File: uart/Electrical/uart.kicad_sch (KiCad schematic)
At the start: 18 parts, among them P2 USB_C_Plug, U1 AP2112K-3.3, U2 FT232RL

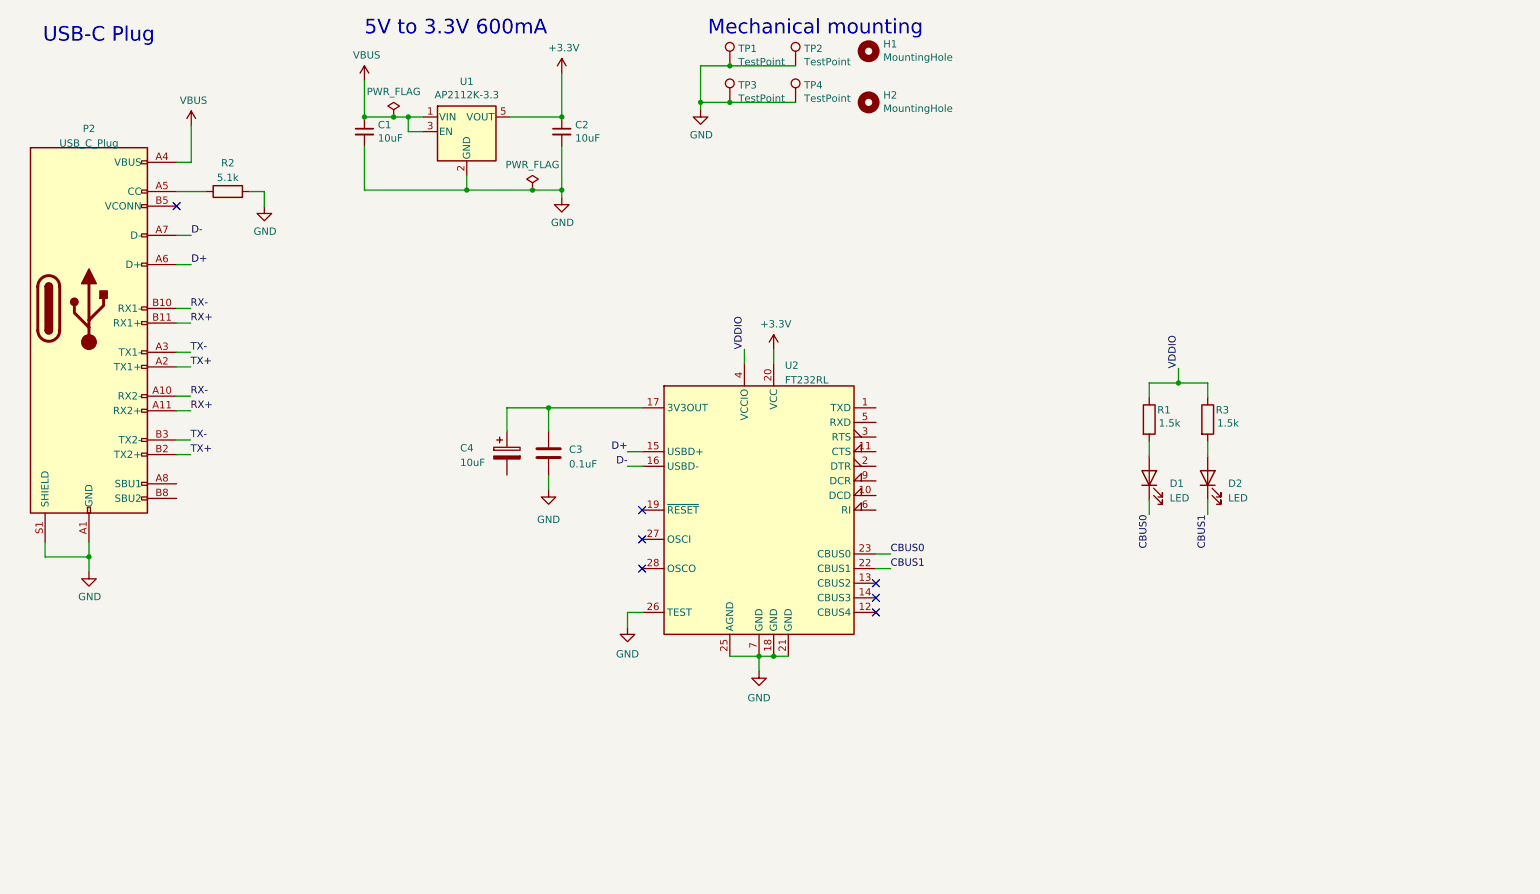
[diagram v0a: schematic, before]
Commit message: Updated uart schematic
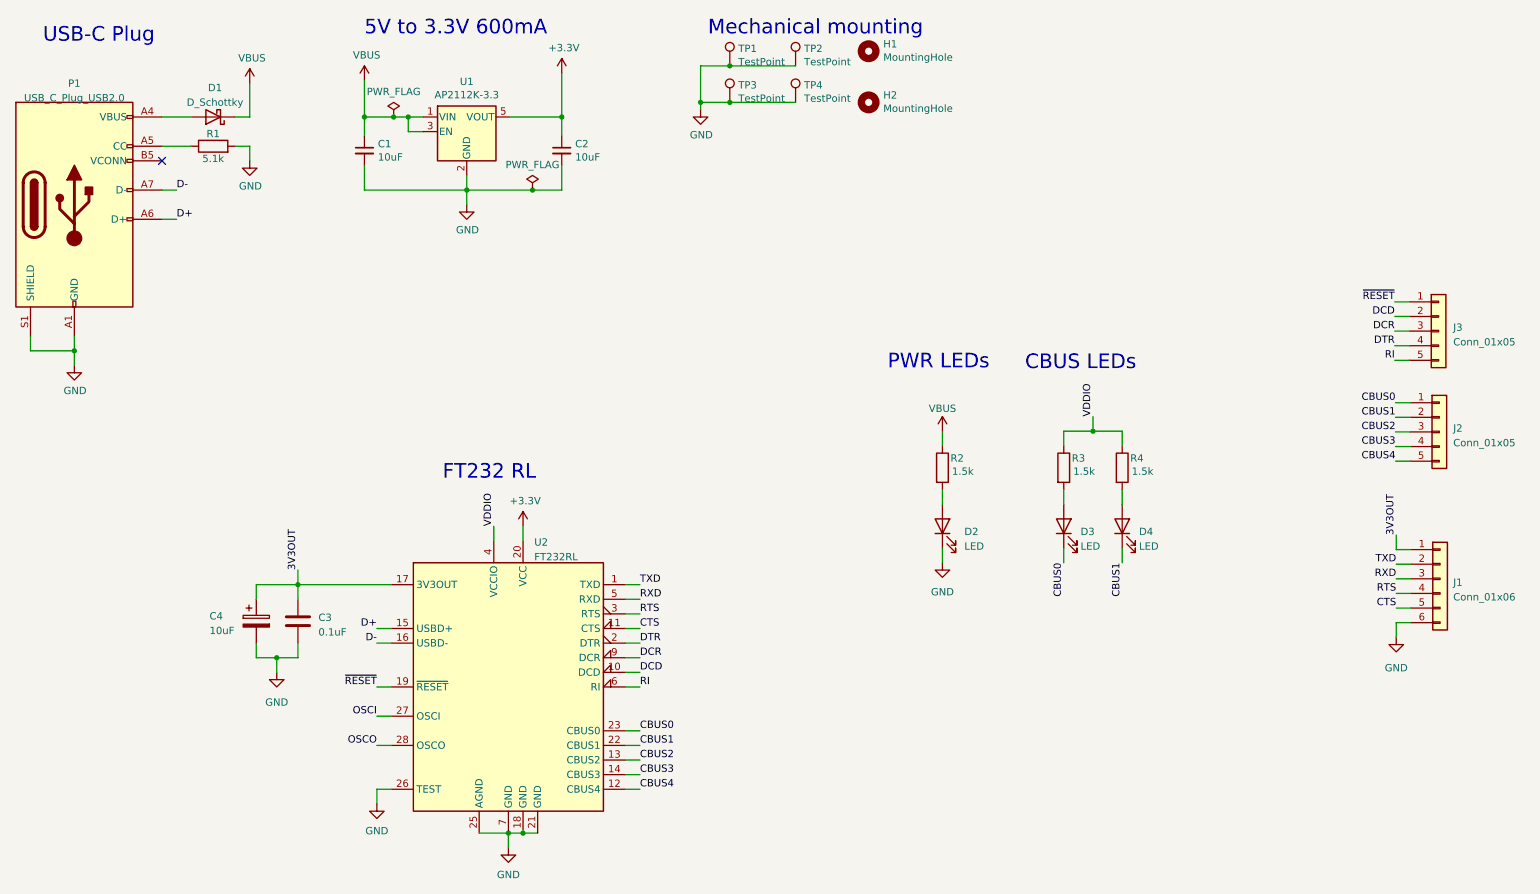
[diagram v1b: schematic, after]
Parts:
- removed P2: USB_C_Plug, Connector_USB:USB_C_Plug_Molex_105444, symbol Connector:USB_C_Plug
- added D1: D_Schottky, Diode_SMD:D_0201_0603Metric, symbol Device:D_Schottky
- added D2: LED, LED_SMD:LED_0201_0603Metric, symbol Device:LED
- added J1: Conn_01x06, Connector_PinHeader_2.00mm:PinHeader_1x06_P2.00mm_Horizontal, symbol Connector_Generic:Conn_01x06
- added J2, J3: Conn_01x05, Connector_PinHeader_2.00mm:PinHeader_1x05_P2.00mm_Vertical, symbol Connector_Generic:Conn_01x05
- added P1: USB_C_Plug_USB2.0, symbol Connector:USB_C_Plug_USB2.0
- added R1: 5.1k, Resistor_SMD:R_0201_0603Metric, symbol Device:R
- R2: value 5.1k -> 1.5k
- TP1, TP2, TP3, TP4: footprint TestPoint:TestPoint_Pad_1.5x1.5mm -> (none)
- renumbered D1 to D3, D2 to D4, R1 to R3, R3 to R4
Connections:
- net CBUS0: now also J2.1 (Pin_1)
- net CBUS1: now also J2.2 (Pin_2)
- net D+: now also P1.A6 (D+)
- net D-: now also P1.A7 (D-)
- net GND: now also C4.2, D2.1 (K), J1.6 (Pin_6), P1.A1 (GND), P1.A12 (GND), P1.B1 (GND), P1.B12 (GND), P1.S1 (SHIELD), R1.2; no longer R2.2
- net VBUS: now also R2.1, D1.1 (K)
- net TXD: now reaches U2.1 (TXD)
- net TXD: now also J1.2 (Pin_2)
- net DCD: now reaches U2.10 (DCD)
- net DCD: now also J3.2 (Pin_2)
- net CTS: now reaches U2.11 (CTS)
- net CTS: now also J1.5 (Pin_5)
- net CBUS4: now reaches U2.12 (CBUS4)
- net CBUS4: now also J2.5 (Pin_5)
- net CBUS2: now reaches U2.13 (CBUS2)
- net CBUS2: now also J2.3 (Pin_3)
- net CBUS3: now reaches U2.14 (CBUS3)
- net CBUS3: now also J2.4 (Pin_4)
- net 3V3OUT: now reaches C3.1, C4.1, U2.17 (3V3OUT)
- net 3V3OUT: now also J1.1 (Pin_1)
- net ~{RESET}: now reaches U2.19 (~{RESET})
- net ~{RESET}: now also J3.1 (Pin_1)
- net DTR: now reaches U2.2 (DTR)
- net DTR: now also J3.4 (Pin_4)
- net OSCI: now reaches U2.27 (OSCI)
- net OSCO: now reaches U2.28 (OSCO)
- net RTS: now reaches U2.3 (RTS)
- net RTS: now also J1.4 (Pin_4)
- net RXD: now reaches U2.5 (RXD)
- net RXD: now also J1.3 (Pin_3)
- net RI: now reaches U2.6 (RI)
- net RI: now also J3.5 (Pin_5)
- net DCR: now reaches U2.9 (DCR)
- net DCR: now also J3.3 (Pin_3)
- new net: D2.2 (A), R2.2
- new net: D1.2 (A), P1.A4 (VBUS), P1.A9 (VBUS), P1.B4 (VBUS), P1.B9 (VBUS)
- new net: P1.A5 (CC), R1.1
- no-connect marks 7 -> 1
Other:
- note added: "CBUS LEDs"
- note added: "FT232 RL"
- note added: "PWR LEDs"
- company: Framework -> (none)
- moved on the sheet: C1, C2, C3, C4, D3, D4, R3, R4, U2

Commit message: Updated uart Schematic
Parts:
- removed J2, J3: Conn_01x05, Connector_PinHeader_2.00mm:PinHeader_1x05_P2.00mm_Vertical, symbol Connector_Generic:Conn_01x05
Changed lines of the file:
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@@
-    (stroke (width 0) (type default))
-  )
-  (wire (pts (xy 260.35 70.231) (xy 262.89 70.231))
     (stroke (width 0) (type default))
   )
@@
     (stroke (width 0) (type default))
   )
-  (wire (pts (xy 260.35 67.691) (xy 262.89 67.691))
-    (stroke (width 0) (type default))
-  )
-  (wire (pts (xy 260.477 90.297) (xy 263.017 90.297))
-    (stroke (width 0) (type default))
-  )
   (wire (pts (xy 83.439 152.4) (xy 83.439 149.86))
     (stroke (width 0) (type default))
@@
     (stroke (width 0) (type default))
   )
-  (wire (pts (xy 260.477 87.757) (xy 263.017 87.757))
-    (stroke (width 0) (type default))
-  )
   (wire (pts (xy 129.159 147.32) (xy 126.619 147.32))
     (stroke (width 0) (type default))
@@
     (stroke (width 0) (type default))
   )
-  (wire (pts (xy 260.35 75.311) (xy 262.89 75.311))
-    (stroke (width 0) (type default))
-  )
   (wire (pts (xy 181.737 100.33) (xy 181.737 97.79))
     (stroke (width 0) (type default))
@@
     (stroke (width 0) (type default))
   )
-  (wire (pts (xy 260.35 72.771) (xy 262.89 72.771))
-    (stroke (width 0) (type default))
-  )
   (wire (pts (xy 129.159 124.46) (xy 126.619 124.46))
     (stroke (width 0) (type default))
@@
     (stroke (width 0) (type default))
   )
-  (wire (pts (xy 260.35 65.151) (xy 262.89 65.151))
-    (stroke (width 0) (type default))
-  )
   (wire (pts (xy 83.439 137.16) (xy 85.979 137.16))
     (stroke (width 0) (type default))
@@
     (stroke (width 0) (type default))
   )
-  (wire (pts (xy 260.477 92.837) (xy 263.017 92.837))
-    (stroke (width 0) (type default))
-  )
-  (wire (pts (xy 260.477 85.217) (xy 263.017 85.217))
-    (stroke (width 0) (type default))
-  )
   (wire (pts (xy 83.439 132.08) (xy 85.979 132.08))
     (stroke (width 0) (type default))
@@
   )
   (wire (pts (xy 69.723 114.3) (xy 69.723 116.84))
-    (stroke (width 0) (type default))
-  )
-  (wire (pts (xy 260.477 82.677) (xy 263.017 82.677))
     (stroke (width 0) (type default))
   )
@@
     (effects (font (size 1.27 1.27)) (justify left bottom))
   )
-  (label "CBUS3" (at 260.477 90.297 180) (fields_autoplaced)
-    (effects (font (size 1.27 1.27)) (justify right bottom))
-  )
-  (label "RI" (at 260.35 75.311 180) (fields_autoplaced)
-    (effects (font (size 1.27 1.27)) (justify right bottom))
-  )
   (label "CBUS0" (at 202.819 110.49 270) (fields_autoplaced)
     (effects (font (size 1.27 1.27)) (justify right bottom))
   )
-  (label "~{RESET}" (at 260.35 65.151 180) (fields_autoplaced)
-    (effects (font (size 1.27 1.27)) (justify right bottom))
-  )
   (label "DCR" (at 129.159 127 0) (fields_autoplaced)
     (effects (font (size 1.27 1.27)) (justify left bottom))
@@
   (label "D-" (at 48.641 45.72 0) (fields_autoplaced)
     (effects (font (size 1.27 1.27)) (justify left bottom))
-  )
-  (label "DTR" (at 260.35 72.771 180) (fields_autoplaced)
-    (effects (font (size 1.27 1.27)) (justify right bottom))
   )
   (label "~{RESET}" (at 83.439 132.08 180) (fields_autoplaced)
@@
     (effects (font (size 1.27 1.27)) (justify left bottom))
   )
-  (label "DCR" (at 260.35 70.231 180) (fields_autoplaced)
-    (effects (font (size 1.27 1.27)) (justify right bottom))
-  )
   (label "CTS" (at 129.159 121.92 0) (fields_autoplaced)
     (effects (font (size 1.27 1.27)) (justify left bottom))
@@
     (effects (font (size 1.27 1.27)) (justify right bottom))
   )
-  (label "DCD" (at 260.35 67.691 180) (fields_autoplaced)
-    (effects (font (size 1.27 1.27)) (justify right bottom))
-  )
   (label "3V3OUT" (at 260.604 105.664 90) (fields_autoplaced)
     (effects (font (size 1.27 1.27)) (justify left bottom))
-  )
-  (label "CBUS1" (at 260.477 85.217 180) (fields_autoplaced)
-    (effects (font (size 1.27 1.27)) (justify right bottom))
   )
   (label "CBUS0" (at 129.159 139.7 0) (fields_autoplaced)
@@
     (effects (font (size 1.27 1.27)) (justify right bottom))
   )
-  (label "CBUS4" (at 260.477 92.837 180) (fields_autoplaced)
-    (effects (font (size 1.27 1.27)) (justify right bottom))
-  )
   (label "D+" (at 48.641 50.8 0) (fields_autoplaced)
     (effects (font (size 1.27 1.27)) (justify left bottom))
@@
     (effects (font (size 1.27 1.27)) (justify right bottom))
   )
-  (label "CBUS2" (at 260.477 87.757 180) (fields_autoplaced)
-    (effects (font (size 1.27 1.27)) (justify right bottom))
-  )
   (label "CBUS2" (at 129.159 144.78 0) (fields_autoplaced)
     (effects (font (size 1.27 1.27)) (justify left bottom))
@@
   (label "DTR" (at 129.159 124.46 0) (fields_autoplaced)
     (effects (font (size 1.27 1.27)) (justify left bottom))
-  )
-  (label "CBUS0" (at 260.477 82.677 180) (fields_autoplaced)
-    (effects (font (size 1.27 1.27)) (justify right bottom))
   )
   (label "OSCO" (at 83.439 142.24 180) (fields_autoplaced)
@@
         (path "/21020eba-b649-4135-9bee-384d0a5cab58"
           (reference "R4") (unit 1)
-        )
-      )
-    )
-  )
-  (symbol (lib_id "Connector_Generic:Conn_01x05") (at 267.97 70.231 0) (unit 1)
-    (in_bom yes) (on_board yes) (dnp no) (fields_autoplaced)
-    (property "Reference" "J3" (at 270.51 69.596 0)
-      (effects (font (size 1.27 1.27)) (justify left))
-    )
-    (property "Value" "Conn_01x05" (at 270.51 72.136 0)
-      (effects (font (size 1.27 1.27)) (justify left))
-    )
-    (property "Footprint" "Connector_PinHeader_2.00mm:PinHeader_1x05_P2.00mm_Vertical" (at 267.97 70.231 0)
-      (effects (font (size 1.27 1.27)) hide)
-    )
-    (property "Datasheet" "~" (at 267.97 70.231 0)
-      (effects (font (size 1.27 1.27)) hide)
-    )
-    (pin "1")
-    (pin "2")
-    (pin "3")
-    (pin "4")
-    (pin "5")
-    (instances
-      (project "uart"
-        (path "/21020eba-b649-4135-9bee-384d0a5cab58"
-          (reference "J3") (unit 1)
         )
       )
@@
         )
       )
-    )
-  )
-  (symbol (lib_id "Connector_Generic:Conn_01x05") (at 268.097 87.757 0) (unit 1)
-    (in_bom yes) (on_board yes) (dnp no) (fields_autoplaced)
-    (property "Reference" "J2" (at 270.51 87.122 0)
-      (effects (font (size 1.27 1.27)) (justify left))
-    )
-    (property "Value" "Conn_01x05" (at 270.51 89.662 0)
-      (effects (font (size 1.27 1.27)) (justify left))
-    )
-    (property "Footprint" "Connector_PinHeader_2.00mm:PinHeader_1x05_P2.00mm_Vertical" (at 268.097 87.757 0)
-      (effects (font (size 1.27 1.27)) hide)
-    )
-    (property "Datasheet" "~" (at 268.097 87.757 0)
-      (effects (font (size 1.27 1.27)) hide)
-    )
-    (pin "1")
-    (pin "2")
-    (pin "3")
-    (pin "4")
-    (pin "5")
-    (instances
-      (project "uart"
-        (path "/21020eba-b649-4135-9bee-384d0a5cab58"
-          (reference "J2") (unit 1)
-        )
-      )

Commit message: Updated UART PCB
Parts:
- removed D3, D4: LED, LED_SMD:LED_0201_0603Metric, symbol Device:LED
- removed R3, R4: 1.5k, Resistor_SMD:R_0201_0603Metric, symbol Device:R
- C1, C2, C3, C4: footprint Capacitor_SMD:C_0805_2012Metric -> Capacitor_SMD:C_0603_1608Metric_Pad1.08x0.95mm_HandSolder
- D1: footprint Diode_SMD:D_0201_0603Metric -> Diode_SMD:D_0603_1608Metric_Pad1.05x0.95mm_HandSolder
- D2: footprint LED_SMD:LED_0201_0603Metric -> LED_SMD:LED_0603_1608Metric_Pad1.05x0.95mm_HandSolder
- J1: footprint Connector_PinHeader_2.00mm:PinHeader_1x06_P2.00mm_Horizontal -> Connector_PinSocket_2.54mm:PinSocket_1x06_P2.54mm_Horizontal
- R1, R2: footprint Resistor_SMD:R_0201_0603Metric -> Resistor_SMD:R_0603_1608Metric_Pad0.98x0.95mm_HandSolder
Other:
- note removed: "CBUS LEDs"
